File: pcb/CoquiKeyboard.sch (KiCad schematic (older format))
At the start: 1 part

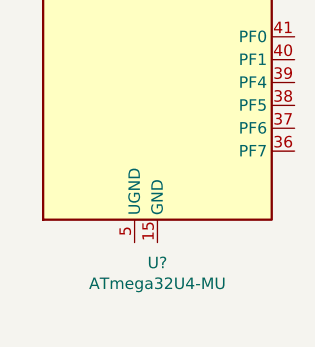
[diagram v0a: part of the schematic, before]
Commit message: attach power and ground to mcu
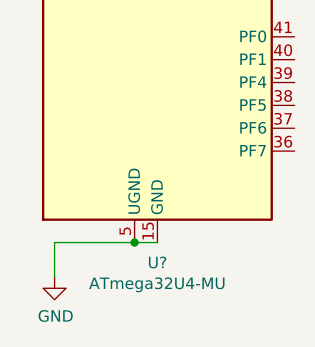
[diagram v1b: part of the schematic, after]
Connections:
- net GND: now reaches U?.15 (GND), U?.23 (GND), U?.35 (GND), U?.43 (GND), U?.45 (GND)
- net GND: now also U?.5 (UGND)
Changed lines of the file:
@@
 Wire Wire Line
 	7350 1450 7250 1450
+$Comp
+L power:GND #PWR?
+U 1 1 5CDE37FF
+P 6900 5200
+F 0 "#PWR?" H 6900 4950 50  0001 C CNN
+F 1 "GND" H 6905 5027 50  0000 C CNN
+F 2 "" H 6900 5200 50  0001 C CNN
+F 3 "" H 6900 5200 50  0001 C CNN
+	1    6900 5200
+	1    0    0    -1
+$EndComp
+Wire Wire Line
+	7350 5050 7250 5050
+Wire Wire Line
+	6900 5050 6900 5200
+Connection ~ 7250 5050
+Wire Wire Line
+	7250 5050 6900 5050
 $EndSCHEMATC

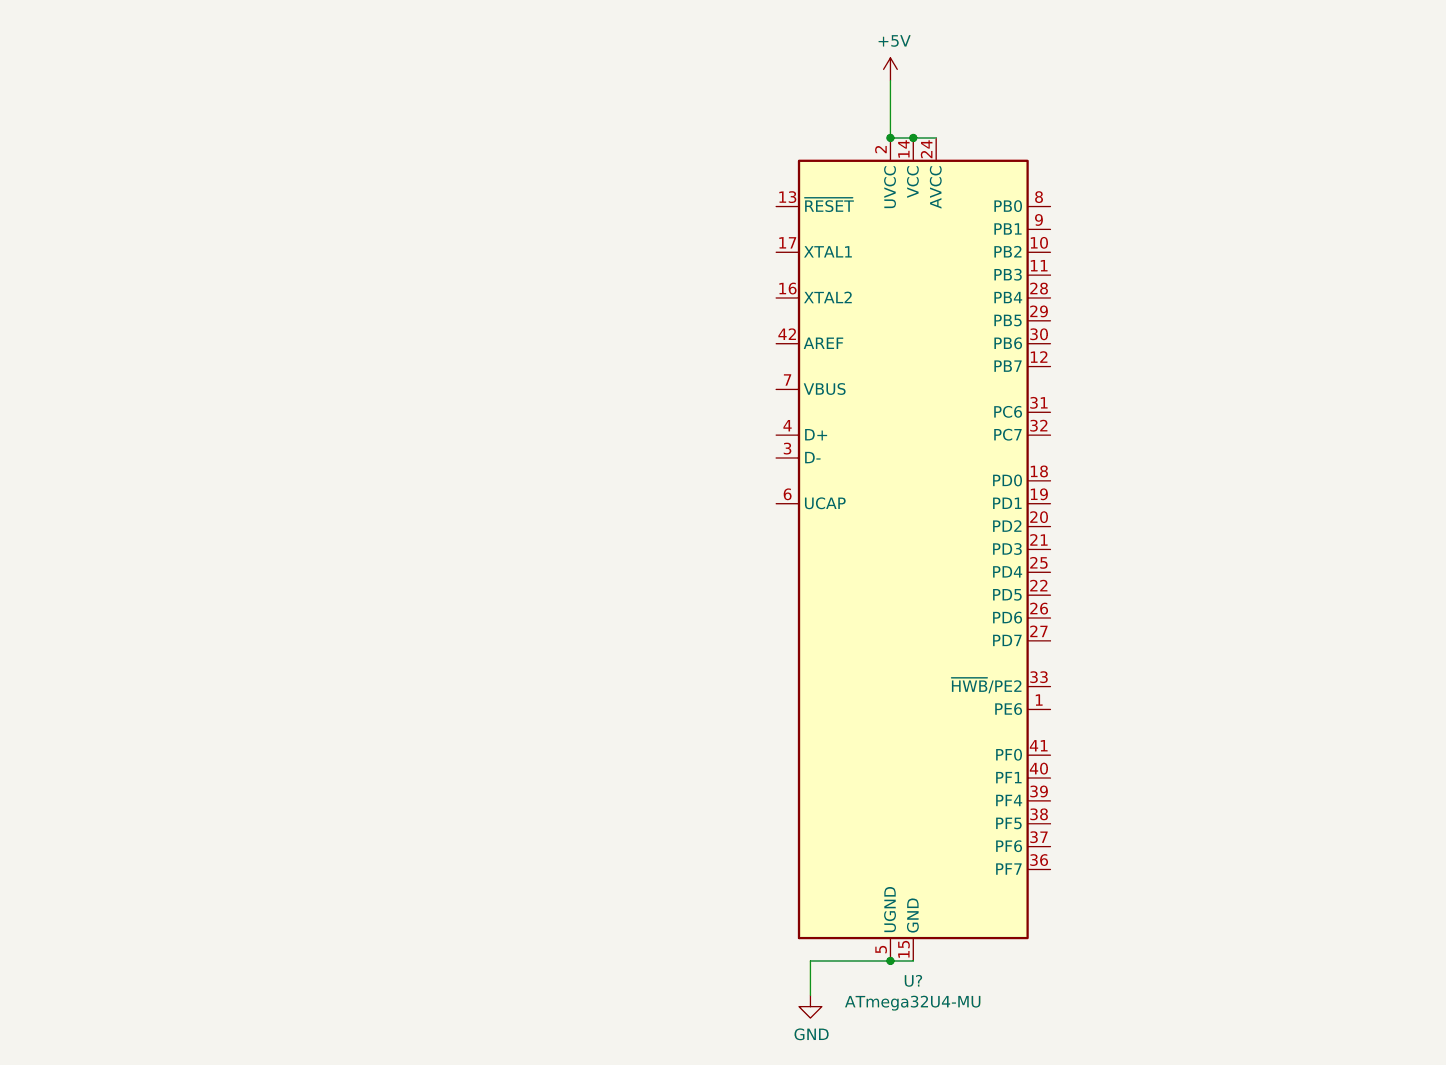
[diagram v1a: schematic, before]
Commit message: add resistors to USB pins
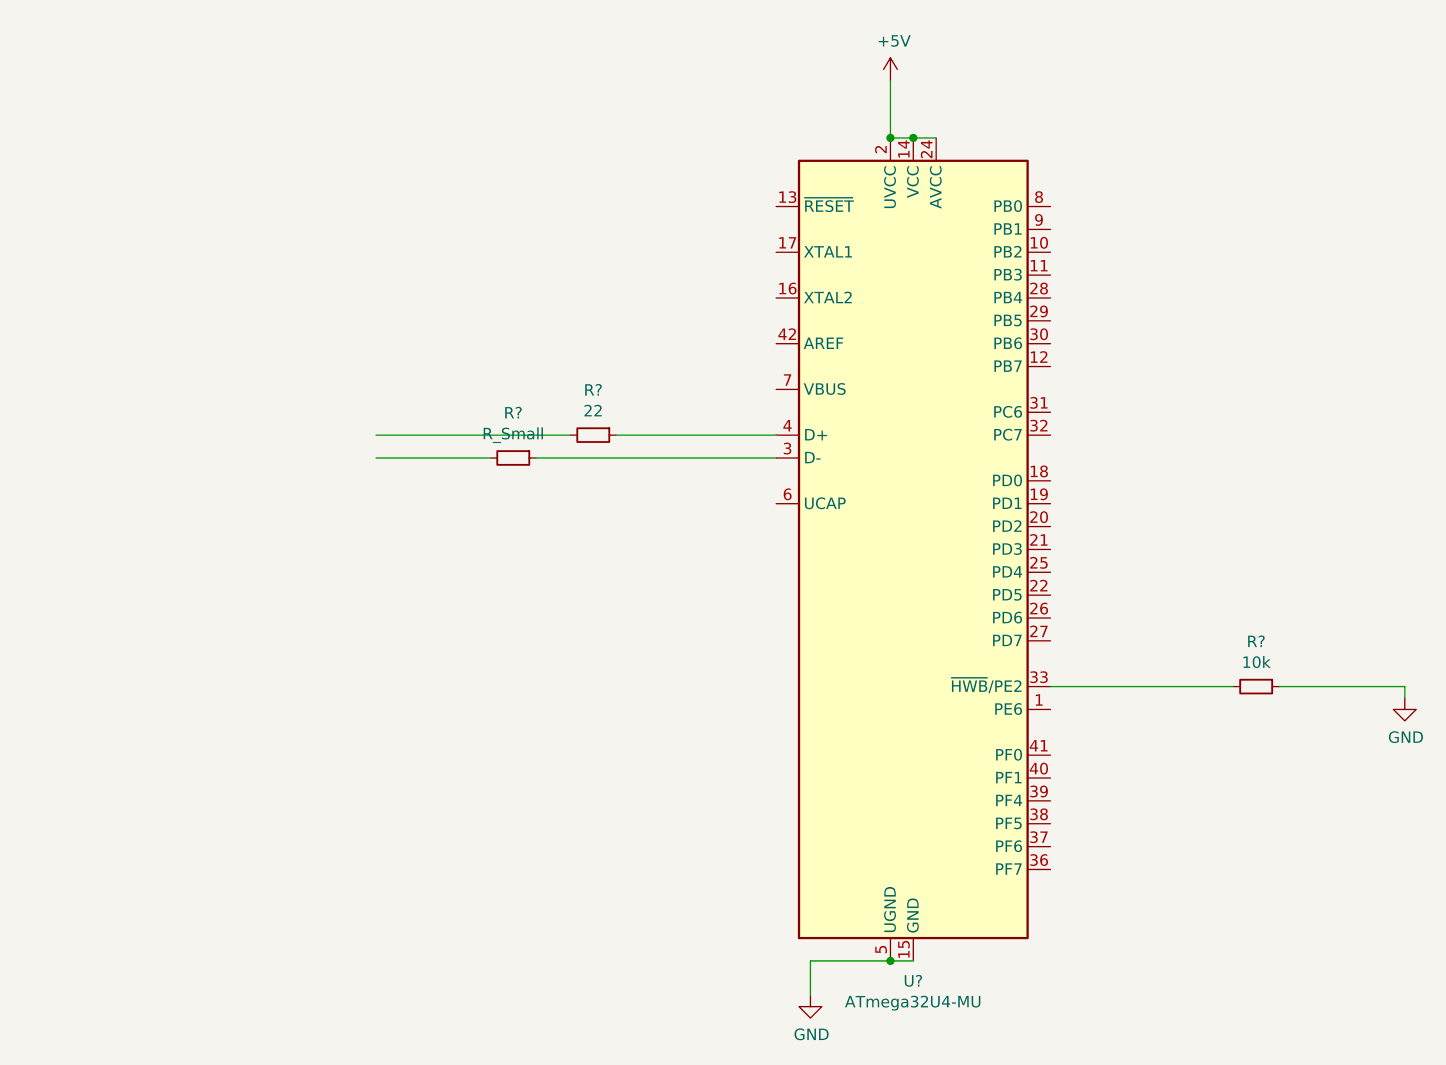
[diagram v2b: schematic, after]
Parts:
- added R?: 10k, symbol Device:R_Small
- added R?: 22, symbol Device:R_Small
- added R?: R_Small, symbol Device:R_Small
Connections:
- wire segments 6 -> 13
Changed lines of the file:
@@
 Wire Wire Line
 	7250 5050 6900 5050
+$Comp
+L Device:R_Small R?
+U 1 1 5CDE412E
+P 8850 3850
+F 0 "R?" V 8654 3850 50  0000 C CNN
+F 1 "10k" V 8745 3850 50  0000 C CNN
+F 2 "" H 8850 3850 50  0001 C CNN
+F 3 "~" H 8850 3850 50  0001 C CNN
+	1    8850 3850
+	0    1    1    0
+$EndComp
+$Comp
+L power:GND #PWR?
+U 1 1 5CDE76C1
+P 9500 3900
+F 0 "#PWR?" H 9500 3650 50  0001 C CNN
+F 1 "GND" H 9505 3727 50  0000 C CNN
+F 2 "" H 9500 3900 50  0001 C CNN
+F 3 "" H 9500 3900 50  0001 C CNN
+	1    9500 3900
+	1    0    0    -1
+$EndComp
+Wire Wire Line
+	7950 3850 8750 3850
+Wire Wire Line
+	9500 3850 9500 3900
+Wire Wire Line
+	8950 3850 9500 3850
+$Comp
+L Device:R_Small R?
+U 1 1 5CDEB80E
+P 5950 2750
+F 0 "R?" V 5754 2750 50  0000 C CNN
+F 1 "22" V 5845 2750 50  0000 C CNN
+F 2 "" H 5950 2750 50  0001 C CNN
+F 3 "~" H 5950 2750 50  0001 C CNN
+	1    5950 2750
+	0    1    1    0
+$EndComp
+$Comp
+L Device:R_Small R?
+U 1 1 5CDEC125
+P 5600 2850
+F 0 "R?" V 5404 2850 50  0000 C CNN
+F 1 "R_Small" V 5495 2850 50  0000 C CNN
+F 2 "" H 5600 2850 50  0001 C CNN
+F 3 "~" H 5600 2850 50  0001 C CNN
+	1    5600 2850
+	0    1    1    0
+$EndComp
+Wire Wire Line
+	6750 2850 5700 2850
+Wire Wire Line
+	5500 2850 5000 2850
+Wire Wire Line
+	6750 2750 6050 2750
+Wire Wire Line
+	5850 2750 5000 2750
 $EndSCHEMATC

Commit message: add capacitors to UCAP
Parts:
- added C?: C_Small, symbol Device:C_Small
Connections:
- wire segments 13 -> 15
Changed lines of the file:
@@
 Wire Wire Line
 	5850 2750 5000 2750
+$Comp
+L Device:C_Small C?
+U 1 1 5CDEDEFF
+P 6000 3150
+F 0 "C?" H 6092 3196 50  0000 L CNN
+F 1 "C_Small" H 6092 3105 50  0000 L CNN
+F 2 "" H 6000 3150 50  0001 C CNN
+F 3 "~" H 6000 3150 50  0001 C CNN
+	1    6000 3150
+	1    0    0    -1
+$EndComp
+$Comp
+L power:GND #PWR?
+U 1 1 5CDEECEE
+P 6000 3400
+F 0 "#PWR?" H 6000 3150 50  0001 C CNN
+F 1 "GND" H 6005 3227 50  0000 C CNN
+F 2 "" H 6000 3400 50  0001 C CNN
+F 3 "" H 6000 3400 50  0001 C CNN
+	1    6000 3400
+	1    0    0    -1
+$EndComp
+Wire Wire Line
+	6750 3050 6000 3050
+Wire Wire Line
+	6000 3250 6000 3400
 $EndSCHEMATC

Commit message: add decoupling capacitors
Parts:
- added C? (x3): 0.1uF, symbol Device:C_Small
- added C?: 10uF, symbol Device:C_Small
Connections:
- wire segments 15 -> 25
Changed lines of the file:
@@
 EESchema Schematic File Version 4
+LIBS:CoquiKeyboard-cache
 EELAYER 29 0
 EELAYER END
@@
 Wire Wire Line
 	6000 3250 6000 3400
+$Comp
+L power:+5V #PWR?
+U 1 1 5CDF4D90
+P 4000 3050
+F 0 "#PWR?" H 4000 2900 50  0001 C CNN
+F 1 "+5V" H 4015 3223 50  0000 C CNN
+F 2 "" H 4000 3050 50  0001 C CNN
+F 3 "" H 4000 3050 50  0001 C CNN
+	1    4000 3050
+	1    0    0    -1
+$EndComp
+$Comp
+L power:GND #PWR?
+U 1 1 5CDF55C6
+P 4000 3550
+F 0 "#PWR?" H 4000 3300 50  0001 C CNN
+F 1 "GND" H 4005 3377 50  0000 C CNN
+F 2 "" H 4000 3550 50  0001 C CNN
+F 3 "" H 4000 3550 50  0001 C CNN
+	1    4000 3550
+	1    0    0    -1
+$EndComp
+$Comp
+L Device:C_Small C?
+U 1 1 5CDF8B07
+P 3500 3300
+F 0 "C?" H 3592 3346 50  0000 L CNN
+F 1 "0.1uF" H 3592 3255 50  0000 L CNN
+F 2 "" H 3500 3300 50  0001 C CNN
+F 3 "~" H 3500 3300 50  0001 C CNN
+	1    3500 3300
+	1    0    0    -1
+$EndComp
+$Comp
+L Device:C_Small C?
+U 1 1 5CDFA63A
+P 3800 3300
+F 0 "C?" H 3892 3346 50  0000 L CNN
+F 1 "0.1uF" H 3892 3255 50  0000 L CNN
+F 2 "" H 3800 3300 50  0001 C CNN
+F 3 "~" H 3800 3300 50  0001 C CNN
+	1    3800 3300
+	1    0    0    -1
+$EndComp
+$Comp
+L Device:C_Small C?
+U 1 1 5CDFA909
+P 4150 3300
+F 0 "C?" H 4242 3346 50  0000 L CNN
+F 1 "0.1uF" H 4242 3255 50  0000 L CNN
+F 2 "" H 4150 3300 50  0001 C CNN
+F 3 "~" H 4150 3300 50  0001 C CNN
+	1    4150 3300
+	1    0    0    -1
+$EndComp
+$Comp
+L Device:C_Small C?
+U 1 1 5CDFAC49
+P 4400 3300
+F 0 "C?" H 4492 3346 50  0000 L CNN
+F 1 "10uF" H 4492 3255 50  0000 L CNN
+F 2 "" H 4400 3300 50  0001 C CNN
+F 3 "~" H 4400 3300 50  0001 C CNN
+	1    4400 3300
+	1    0    0    -1
+$EndComp
+Connection ~ 3800 3200
+Wire Wire Line
+	3800 3200 4000 3200
+Wire Wire Line
+	4000 3050 4000 3200
+Connection ~ 4000 3200
+Wire Wire Line
+	4000 3200 4150 3200
+Connection ~ 3800 3400
+Wire Wire Line
+	3800 3400 4000 3400
+Wire Wire Line
+	4000 3550 4000 3400
+Connection ~ 4000 3400
+Wire Wire Line
+	4000 3400 4150 3400
+Wire Wire Line
+	3500 3200 3800 3200
+Wire Wire Line
+	3500 3400 3800 3400
+Connection ~ 4150 3200
+Connection ~ 4150 3400
+Wire Wire Line
+	4150 3200 4400 3200
+Wire Wire Line
+	4150 3400 4400 3400
 $EndSCHEMATC

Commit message: bind VBUS to 5V
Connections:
- wire segments 25 -> 26
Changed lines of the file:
@@
 Wire Wire Line
 	4150 3400 4400 3400
+$Comp
+L power:+5V #PWR?
+U 1 1 5CE11A4D
+P 6200 2550
+F 0 "#PWR?" H 6200 2400 50  0001 C CNN
+F 1 "+5V" H 6215 2723 50  0000 C CNN
+F 2 "" H 6200 2550 50  0001 C CNN
+F 3 "" H 6200 2550 50  0001 C CNN
+	1    6200 2550
+	1    0    0    -1
+$EndComp
+Wire Wire Line
+	6750 2550 6200 2550
 $EndSCHEMATC

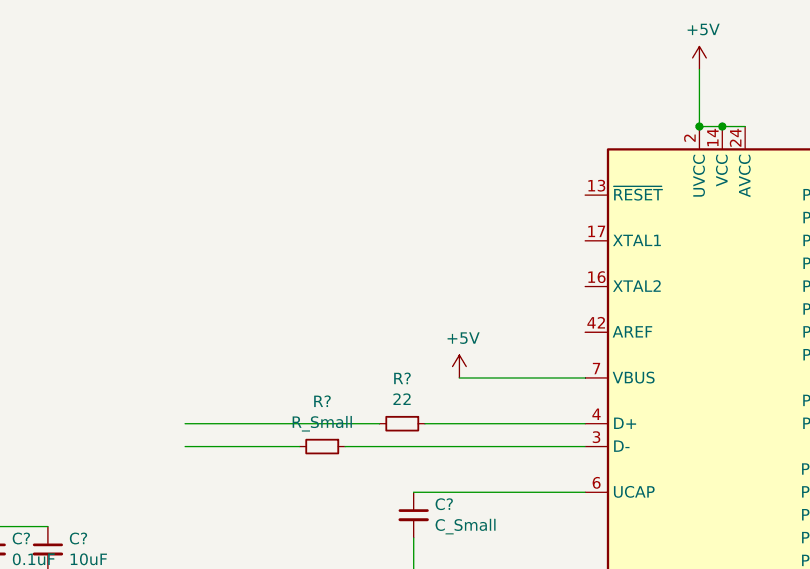
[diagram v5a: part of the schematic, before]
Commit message: add crystal with load capacitors
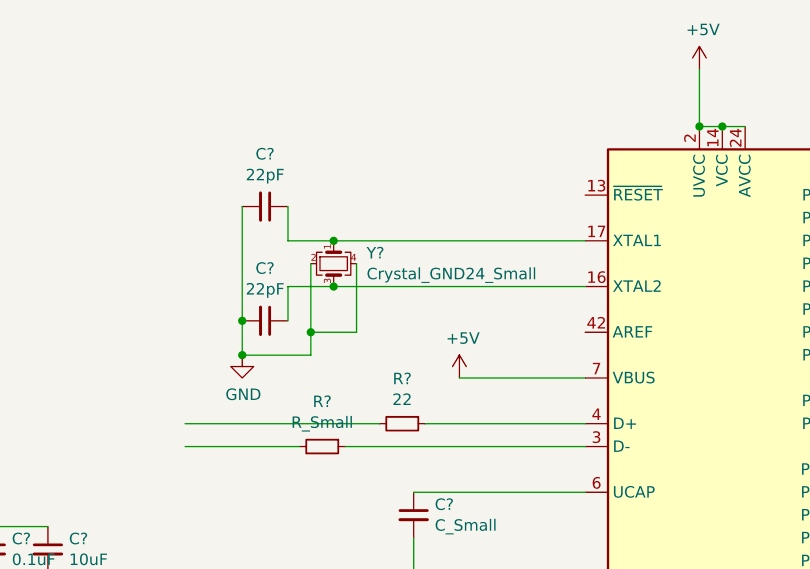
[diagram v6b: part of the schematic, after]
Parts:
- added C? (x2): 22pF, symbol Device:C_Small
- added Y?: Crystal_GND24_Small, symbol Device:Crystal_GND24_Small
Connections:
- wire segments 26 -> 39
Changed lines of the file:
@@
 Wire Wire Line
 	6750 2550 6200 2550
+$Comp
+L Device:Crystal_GND24_Small Y?
+U 1 1 5CE138C0
+P 5650 2050
+F 0 "Y?" V 5604 2194 50  0000 L CNN
+F 1 "Crystal_GND24_Small" V 5695 2194 50  0000 L CNN
+F 2 "" H 5650 2050 50  0001 C CNN
+F 3 "~" H 5650 2050 50  0001 C CNN
+	1    5650 2050
+	0    1    1    0
+$EndComp
+Wire Wire Line
+	5650 1950 6750 1950
+$Comp
+L Device:C_Small C?
+U 1 1 5CE17419
+P 5350 1800
+F 0 "C?" V 5121 1800 50  0000 C CNN
+F 1 "22pF" V 5212 1800 50  0000 C CNN
+F 2 "" H 5350 1800 50  0001 C CNN
+F 3 "~" H 5350 1800 50  0001 C CNN
+	1    5350 1800
+	0    1    1    0
+$EndComp
+$Comp
+L Device:C_Small C?
+U 1 1 5CE17DB6
+P 5350 2300
+F 0 "C?" V 5121 2300 50  0000 C CNN
+F 1 "22pF" V 5212 2300 50  0000 C CNN
+F 2 "" H 5350 2300 50  0001 C CNN
+F 3 "~" H 5350 2300 50  0001 C CNN
+	1    5350 2300
+	0    1    1    0
+$EndComp
+Wire Wire Line
+	5650 1950 5450 1950
+Wire Wire Line
+	5450 1950 5450 1800
+Connection ~ 5650 1950
+Wire Wire Line
+	5550 2050 5550 2350
+Wire Wire Line
+	5750 2050 5750 2350
+Wire Wire Line
+	5750 2350 5550 2350
+$Comp
+L power:GND #PWR?
+U 1 1 5CE2576A
+P 5250 2450
+F 0 "#PWR?" H 5250 2200 50  0001 C CNN
+F 1 "GND" H 5255 2277 50  0000 C CNN
+F 2 "" H 5250 2450 50  0001 C CNN
+F 3 "" H 5250 2450 50  0001 C CNN
+	1    5250 2450
+	1    0    0    -1
+$EndComp
+Wire Wire Line
+	5250 1800 5250 2300
+Connection ~ 5250 2300
+Wire Wire Line
+	5250 2300 5250 2450
+Wire Wire Line
+	5450 2300 5450 2150
+Wire Wire Line
+	5450 2150 5650 2150
+Connection ~ 5650 2150
+Wire Wire Line
+	5650 2150 6750 2150
+Wire Wire Line
+	5550 2350 5550 2450
+Wire Wire Line
+	5550 2450 5250 2450
+Connection ~ 5550 2350
+Connection ~ 5250 2450
 $EndSCHEMATC

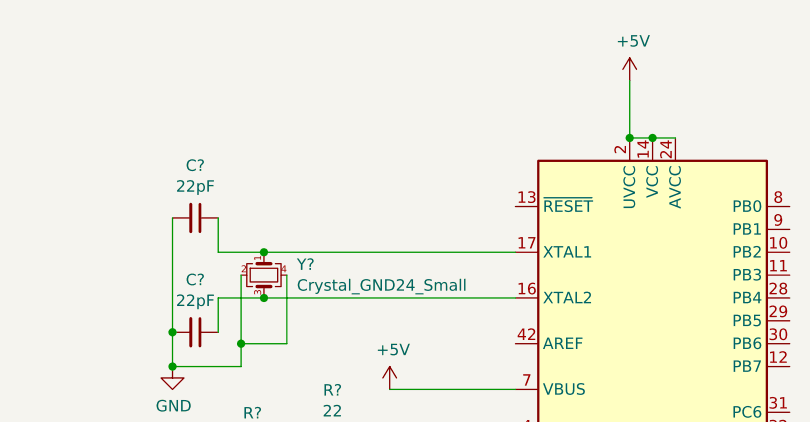
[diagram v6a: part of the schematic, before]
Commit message: add pull up resistor between reset and +5v
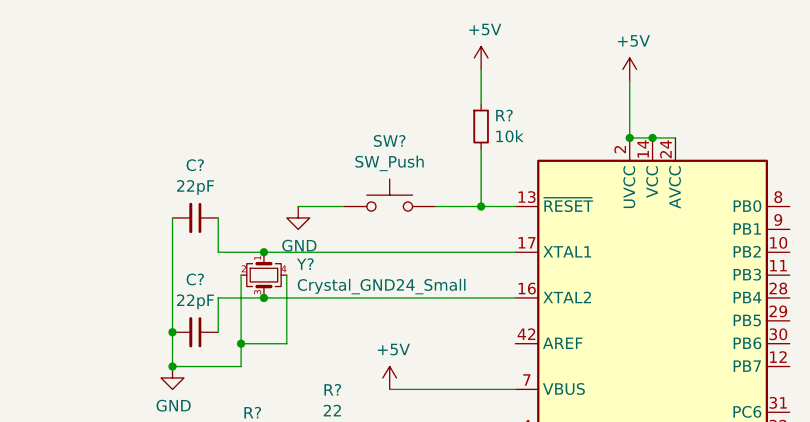
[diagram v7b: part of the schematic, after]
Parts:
- added R?: 10k, symbol Device:R_Small
- added SW?: SW_Push, symbol Switch:SW_Push
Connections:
- wire segments 39 -> 44
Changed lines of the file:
@@
 Connection ~ 5550 2350
 Connection ~ 5250 2450
+$Comp
+L Switch:SW_Push SW?
+U 1 1 5CE2FBD9
+P 6200 1750
+F 0 "SW?" H 6200 2035 50  0000 C CNN
+F 1 "SW_Push" H 6200 1944 50  0000 C CNN
+F 2 "" H 6200 1950 50  0001 C CNN
+F 3 "~" H 6200 1950 50  0001 C CNN
+	1    6200 1750
+	1    0    0    -1
+$EndComp
+$Comp
+L power:GND #PWR?
+U 1 1 5CE30BA9
+P 5800 1750
+F 0 "#PWR?" H 5800 1500 50  0001 C CNN
+F 1 "GND" H 5805 1577 50  0000 C CNN
+F 2 "" H 5800 1750 50  0001 C CNN
+F 3 "" H 5800 1750 50  0001 C CNN
+	1    5800 1750
+	1    0    0    -1
+$EndComp
+Wire Wire Line
+	6400 1750 6600 1750
+Wire Wire Line
+	6000 1750 5800 1750
+$Comp
+L Device:R_Small R?
+U 1 1 5CE3800D
+P 6600 1400
+F 0 "R?" H 6659 1446 50  0000 L CNN
+F 1 "10k" H 6659 1355 50  0000 L CNN
+F 2 "" H 6600 1400 50  0001 C CNN
+F 3 "~" H 6600 1400 50  0001 C CNN
+	1    6600 1400
+	1    0    0    -1
+$EndComp
+Wire Wire Line
+	6600 1750 6600 1500
+Connection ~ 6600 1750
+Wire Wire Line
+	6600 1750 6750 1750
+$Comp
+L power:+5V #PWR?
+U 1 1 5CE3958F
+P 6600 1150
+F 0 "#PWR?" H 6600 1000 50  0001 C CNN
+F 1 "+5V" H 6615 1323 50  0000 C CNN
+F 2 "" H 6600 1150 50  0001 C CNN
+F 3 "" H 6600 1150 50  0001 C CNN
+	1    6600 1150
+	1    0    0    -1
+$EndComp
+Wire Wire Line
+	6600 1300 6600 1150
 $EndSCHEMATC

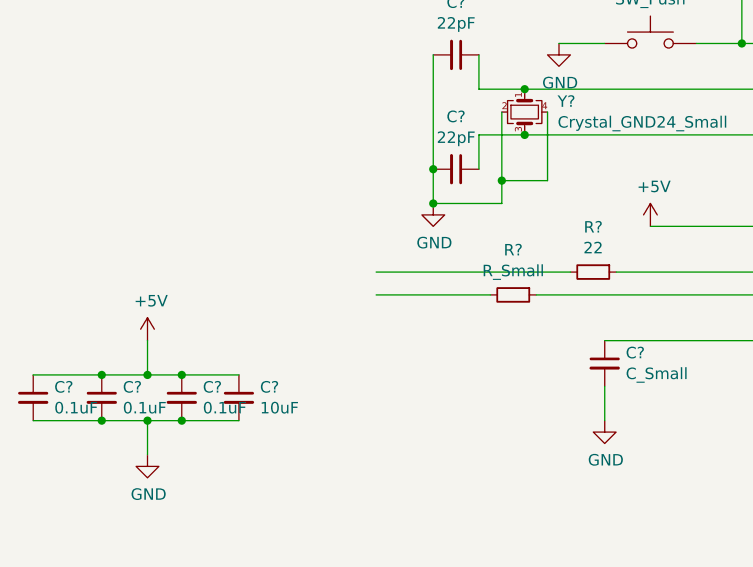
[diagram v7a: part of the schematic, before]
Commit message: place global nets on the USB lines
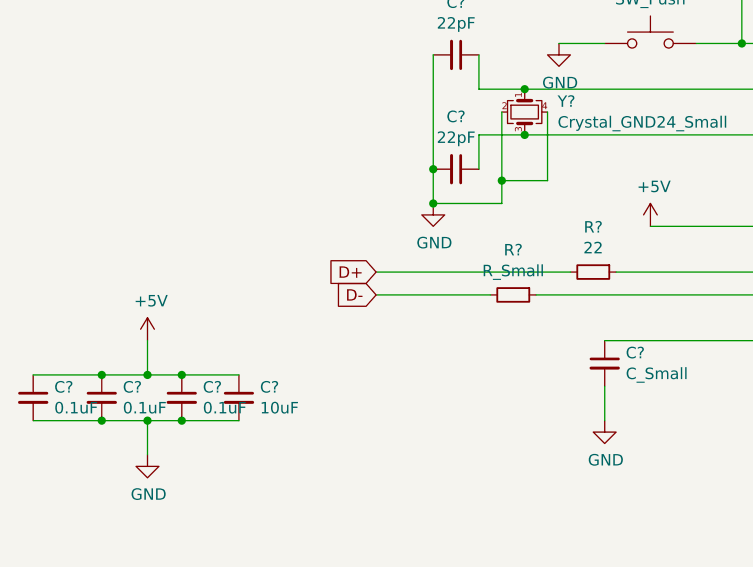
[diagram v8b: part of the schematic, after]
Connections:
- net labels added: D+, D-
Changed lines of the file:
@@
 Wire Wire Line
 	6600 1300 6600 1150
+Text GLabel 5000 2750 0    50   Input ~ 0
+D+
+Text GLabel 5000 2850 0    50   Input ~ 0
+D-
 $EndSCHEMATC
